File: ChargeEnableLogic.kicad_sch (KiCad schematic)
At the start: 28 parts, among them U3 PIC18F16Q20, U4 RX8130CE, U7 SN74CBTLV3257RSVR, U9 GSF7002DW

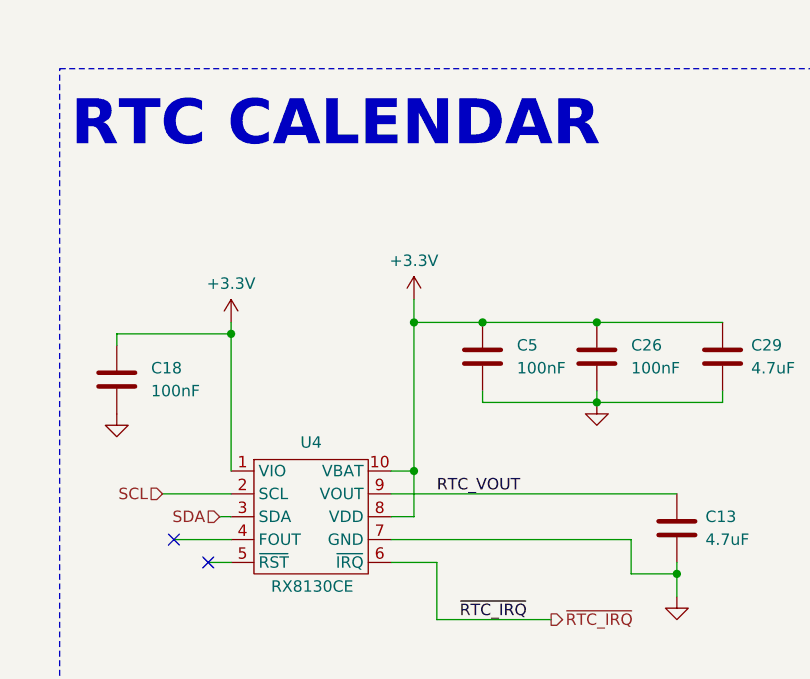
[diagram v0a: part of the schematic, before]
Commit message: fix: modifications after driver completion
- Added missing RTC IRQ to PI
- RTC VBAT is not connected to the Main Battery trough a ~1k resistor
- Connected BQ CE through a Push-pull to Open-Drain converter to PI
- Changed Mosfets to TI PicoStar model
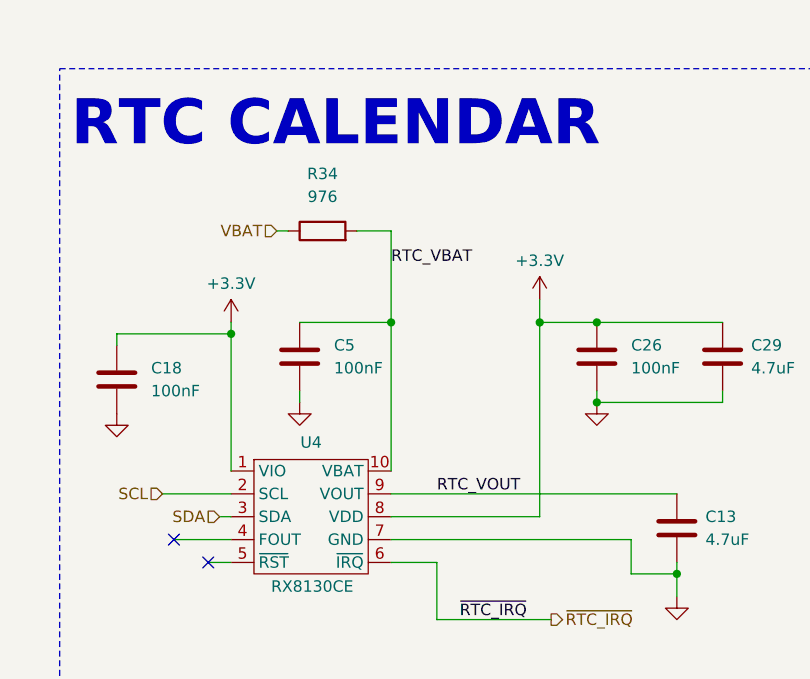
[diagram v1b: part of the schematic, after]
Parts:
- added R34: 976, Resistor_SMD:R_0402_1005Metric, symbol Device:R
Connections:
- net +3.3V: no longer C5.1, U4.10 (VBAT)
- new net RTC_VBAT: C5.1, R34.2, U4.10 (VBAT)
- new net VBAT: R34.1
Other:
- moved on the sheet: C5
